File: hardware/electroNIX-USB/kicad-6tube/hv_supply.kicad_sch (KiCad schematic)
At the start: 25 parts, among them Q3 IRLR3110ZPBF

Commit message: electroNIX-USB: apply RFT Z573M data sheet, add tube footprint
The data book confirms the pinout already in the symbol. The tube is
side-view (not top-view), with 13 flying leads on a 9.53 mm circle and
wire 7 at the front. New footprint electronix:Nixie_RFT_Z573M (top
view, wire 7 toward the front edge) is assigned to the tubes.

Tube current: Ik is 1.5-2.5 mA continuous, 12 mA pulse. PCB-036's 10k
anode resistors averaged only ~0.75 mA per tube when multiplexed. Anode
resistors are now 5k6 (4 tubes) and 3k9 (6 tubes), cathode base
resistors 6k8. To carry the extra HV power, the ladder caps go to
2.2 uF and the 6-tube build uses a 22 uH inductor.

Co-Authored-By: Claude Opus 5.5 <noreply@anthropic.com>
Claude-Session: https://claude.ai/code/session_01AFMfevKEKDGbci8uJGhf4W
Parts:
- C13, C14, C15, C16, C17, C18, C19: value 1u 100V -> 2u2 100V
- L1: value 33u WE 7447715330 -> 22u WE 7447715220
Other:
- note added: "Cockcroft-Walton multiplier, 7 x 10MQ100N, 7 x 2u2/100V (PCB-036 used 1u)"
- note removed: "Cockcroft-Walton multiplier, 7 x 10MQ100N, 7 x 1u/100V (as PCB-036)"
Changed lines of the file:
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@@
       (type none))
 )
-  (text "Cockcroft-Walton multiplier, 7 x 10MQ100N, 7 x 1u/100V (as PCB-036)"
+  (text "Cockcroft-Walton multiplier, 7 x 10MQ100N, 7 x 2u2/100V (PCB-036 used 1u)"
     (at 161.27 26.27 0)
     (effects
@@
           (size 1.27 1.27))
         (justify left)))
-    (property "Value" "33u WE 7447715330"
+    (property "Value" "22u WE 7447715220"
       (at 71.12 50.8 0)
       (effects
@@
         (font
           (size 1.27 1.27))))
-    (property "Value" "1u 100V"
+    (property "Value" "2u2 100V"
       (at 199.39 52.07 90)
       (effects
@@
         (font
           (size 1.27 1.27))))
-    (property "Value" "1u 100V"
+    (property "Value" "2u2 100V"
       (at 250.19 52.07 90)
       (effects
@@
         (font
           (size 1.27 1.27))))
-    (property "Value" "1u 100V"
+    (property "Value" "2u2 100V"
       (at 299.72 52.07 90)
       (effects
@@
         (font
           (size 1.27 1.27))))
-    (property "Value" "1u 100V"
+    (property "Value" "2u2 100V"
       (at 350.52 52.07 90)
       (effects
@@
         (font
           (size 1.27 1.27))))
-    (property "Value" "1u 100V"
+    (property "Value" "2u2 100V"
       (at 224.79 97.79 90)
       (effects
@@
         (font
           (size 1.27 1.27))))
-    (property "Value" "1u 100V"
+    (property "Value" "2u2 100V"
       (at 275.59 97.79 90)
       (effects
@@
         (font
           (size 1.27 1.27))))
-    (property "Value" "1u 100V"
+    (property "Value" "2u2 100V"
       (at 325.12 97.79 90)
       (effects

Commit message: electroNIX-USB: drop all switches, regroup board placement by circuit
- No RESET/BOOT/SET: the firmware reads no button, and the CH340C
  DTR/RTS auto-reset handles flashing. SET's pull-up and cap are gone.
- Boost converter is a compact loop (input caps -> L1 -> FET tab) feeding
  the multiplier columns in chain order.
- ESP32: 3V3 decoupling at pin 2, EN RC at pin 3, HV feedback divider and
  clamp at IO35; auto-reset between the CH340C and the module's UART pins.
- Front band spread out: output cap + KBIAS left, cathode row, one anode
  cluster under each tube.
- 6-tube board placed too (150 x 66 mm). Both boards unrouted.

Co-Authored-By: Claude Opus 5.5 <noreply@anthropic.com>
Claude-Session: https://claude.ai/code/session_01AFMfevKEKDGbci8uJGhf4W
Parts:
- removed C21: 100n, Capacitor_SMD:C_0805_2012Metric, symbol Device:C
- removed R12: 6k2, Resistor_SMD:R_0805_2012Metric, symbol Device:R
- added C10: 22u 10V, Capacitor_SMD:C_1206_3216Metric, symbol Device:C
- added R8: 10R, Resistor_SMD:R_0805_2012Metric, symbol Device:R
- C11: value 22u 10V -> 100n; footprint Capacitor_SMD:C_1206_3216Metric -> Capacitor_SMD:C_0805_2012Metric
- C12: value 100n -> 2u2 100V; footprint Capacitor_SMD:C_0805_2012Metric -> Capacitor_SMD:C_1210_3225Metric
- C19: value 2u2 100V -> 2u2 250V; footprint Capacitor_SMD:C_1210_3225Metric -> Capacitor_THT:CP_Radial_D6.3mm_P2.50mm; symbol Device:C -> Device:C_Polarized
- C20: value 2u2 250V -> 100n; footprint Capacitor_THT:CP_Radial_D6.3mm_P2.50mm -> Capacitor_SMD:C_0805_2012Metric; symbol Device:C_Polarized -> Device:C
- R10: value 10k -> 430k; footprint Resistor_SMD:R_0805_2012Metric -> Resistor_SMD:R_1206_3216Metric
- R11: value 430k -> 6k2; footprint Resistor_SMD:R_1206_3216Metric -> Resistor_SMD:R_0805_2012Metric
- R9: value 10R -> 10k
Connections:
- net +170V: now also C12.1, C19.1, R10.1; no longer C13.1, C20.1, R11.1
- net +5V: now also C10.1; no longer C12.1
- net CW_B1: now also C17.2, C18.1; no longer C18.2, C19.1
- net CW_B2: now also C16.2, C17.1; no longer C17.2, C18.1
- net CW_B3: now also C16.1; no longer C17.1
- net CW_T1: now also C14.2, C15.1; no longer C15.2, C16.1
- net CW_T2: now also C13.2, C14.1; no longer C14.2, C15.1
- net CW_T3: now also C12.2, C13.1; no longer C13.2, C14.1
- net GND: now also C15.2, C19.2, R11.2, R9.2, C10.2; no longer C12.2, C16.2, R10.2
- net HV_SW: now also C18.2; no longer C19.2
- net KOMP_170V: now also C20.1, R10.2, R11.1; no longer R11.2
- net PWM: now also R8.1; no longer R10.1
- net at Q3.1 (G): now also R8.2; no longer R9.2
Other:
- moved on the sheet: C11, C12, C13, C14, C15, C16, C17, C18, R10, R11, R9
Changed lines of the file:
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@@
     (on_board yes)
     (dnp no)
-    (property "Reference" "C11"
+    (property "Reference" "C10"
       (at 36.83 58.42 0)
       (effects
@@
       (project "electroNIX-USB"
         (path "/af167dc7-e2c9-570c-bdf4-28156a519677/f6fa350a-459e-5361-98c1-1f12d068c3cb"
-          (reference "C11")
+          (reference "C10")
           (unit 1)))))
   (symbol
@@
     (on_board yes)
     (dnp no)
-    (property "Reference" "C12"
+    (property "Reference" "C11"
       (at 48.26 58.42 0)
       (effects
@@
       (project "electroNIX-USB"
         (path "/af167dc7-e2c9-570c-bdf4-28156a519677/f6fa350a-459e-5361-98c1-1f12d068c3cb"
-          (reference "C12")
+          (reference "C11")
           (unit 1)))))
   (symbol
@@
     (on_board yes)
     (dnp no)
-    (property "Reference" "R9"
+    (property "Reference" "R8"
       (at 91.44 77.47 90)
       (effects
@@
       (project "electroNIX-USB"
         (path "/af167dc7-e2c9-570c-bdf4-28156a519677/f6fa350a-459e-5361-98c1-1f12d068c3cb"
-          (reference "R9")
+          (reference "R8")
           (unit 1)))))
   (symbol
@@
     (on_board yes)
     (dnp no)
-    (property "Reference" "R10"
+    (property "Reference" "R9"
       (at 86.36 93.98 0)
       (effects
@@
       (project "electroNIX-USB"
         (path "/af167dc7-e2c9-570c-bdf4-28156a519677/f6fa350a-459e-5361-98c1-1f12d068c3cb"
-          (reference "R10")
+          (reference "R9")
           (unit 1)))))
   (symbol
@@
     (on_board yes)
     (dnp no)
-    (property "Reference" "C13"
+    (property "Reference" "C12"
       (at 199.39 46.99 90)
       (effects
@@
       (project "electroNIX-USB"
         (path "/af167dc7-e2c9-570c-bdf4-28156a519677/f6fa350a-459e-5361-98c1-1f12d068c3cb"
-          (reference "C13")
+          (reference "C12")
           (unit 1)))))
   (symbol
@@
     (on_board yes)
     (dnp no)
-    (property "Reference" "C14"
+    (property "Reference" "C13"
       (at 250.19 46.99 90)
       (effects
@@
       (project "electroNIX-USB"
         (path "/af167dc7-e2c9-570c-bdf4-28156a519677/f6fa350a-459e-5361-98c1-1f12d068c3cb"
-          (reference "C14")
+          (reference "C13")
           (unit 1)))))
   (symbol
@@
     (on_board yes)
     (dnp no)
-    (property "Reference" "C15"
+    (property "Reference" "C14"
       (at 299.72 46.99 90)
       (effects
@@
       (project "electroNIX-USB"
         (path "/af167dc7-e2c9-570c-bdf4-28156a519677/f6fa350a-459e-5361-98c1-1f12d068c3cb"
-          (reference "C15")
+          (reference "C14")
           (unit 1)))))
   (symbol
@@
     (on_board yes)
     (dnp no)
-    (property "Reference" "C16"
+    (property "Reference" "C15"
       (at 350.52 46.99 90)
       (effects
@@
       (project "electroNIX-USB"
         (path "/af167dc7-e2c9-570c-bdf4-28156a519677/f6fa350a-459e-5361-98c1-1f12d068c3cb"
-          (reference "C16")
+          (reference "C15")
           (unit 1)))))
   (symbol
@@
     (on_board yes)
     (dnp no)
-    (property "Reference" "C17"
+    (property "Reference" "C16"
       (at 224.79 92.71 90)
       (effects
@@
       (project "electroNIX-USB"
         (path "/af167dc7-e2c9-570c-bdf4-28156a519677/f6fa350a-459e-5361-98c1-1f12d068c3cb"
-          (reference "C17")
+          (reference "C16")
           (unit 1)))))
   (symbol
@@
     (on_board yes)
     (dnp no)
-    (property "Reference" "C18"
+    (property "Reference" "C17"
       (at 275.59 92.71 90)
       (effects
@@
       (project "electroNIX-USB"
         (path "/af167dc7-e2c9-570c-bdf4-28156a519677/f6fa350a-459e-5361-98c1-1f12d068c3cb"
-          (reference "C18")
+          (reference "C17")
           (unit 1)))))
   (symbol
@@
     (on_board yes)
     (dnp no)
-    (property "Reference" "C19"
+    (property "Reference" "C18"
       (at 325.12 92.71 90)
       (effects
@@
       (project "electroNIX-USB"
         (path "/af167dc7-e2c9-570c-bdf4-28156a519677/f6fa350a-459e-5361-98c1-1f12d068c3cb"
-          (reference "C19")
+          (reference "C18")
           (unit 1)))))
   (symbol
@@
     (on_board yes)
     (dnp no)
-    (property "Reference" "C20"
+    (property "Reference" "C19"
       (at 45.72 163.83 0)
       (effects
@@
       (project "electroNIX-USB"
         (path "/af167dc7-e2c9-570c-bdf4-28156a519677/f6fa350a-459e-5361-98c1-1f12d068c3cb"
-          (reference "C20")
+          (reference "C19")
           (unit 1)))))
   (symbol
@@
     (on_board yes)
     (dnp no)
-    (property "Reference" "R11"
+    (property "Reference" "R10"
       (at 101.6 158.75 0)
       (effects
@@
       (project "electroNIX-USB"
         (path "/af167dc7-e2c9-570c-bdf4-28156a519677/f6fa350a-459e-5361-98c1-1f12d068c3cb"
-          (reference "R11")
+          (reference "R10")
           (unit 1)))))
   (symbol
@@
     (on_board yes)
     (dnp no)
-    (property "Reference" "R12"
+    (property "Reference" "R11"
       (at 101.6 179.07 0)
       (effects
@@
       (project "electroNIX-USB"
         (path "/af167dc7-e2c9-570c-bdf4-28156a519677/f6fa350a-459e-5361-98c1-1f12d068c3cb"
-          (reference "R12")
+          (reference "R11")
           (unit 1)))))
   (symbol
@@
     (on_board yes)
     (dnp no)
-    (property "Reference" "C21"
+    (property "Reference" "C20"
       (at 116.84 173.99 0)
       (effects
@@
       (project "electroNIX-USB"
         (path "/af167dc7-e2c9-570c-bdf4-28156a519677/f6fa350a-459e-5361-98c1-1f12d068c3cb"
-          (reference "C21")
-          (unit 1)))))
-  (symbol
+          (reference "C20")
+          (unit 1)))))
+  (symbol

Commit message: electroNIX-USB: boost gate pull-down gate-to-source as on PCB-036
R45 on PCB-036 pulls the FET gate (after the 10R) to GND; ours sat on
the IO2 side. Move it to the gate and place it at the gate pad. Add a
note listing what was checked against the PCB-036 schematic.

Co-Authored-By: Claude Opus 5.5 <noreply@anthropic.com>
Claude-Session: https://claude.ai/code/session_01AFMfevKEKDGbci8uJGhf4W
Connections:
- net PWM: no longer R9.1
- net at Q3.1 (G), R8.2: now also R9.1
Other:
- note added: "IO2 drives the logic-level FET directly, 32 kHz, duty clamped to ~41 % by firmware (HV_DUTY_MAX). 10k gate-source keeps the FET off (and IO2 low) during boot."
- note removed: "IO2 drives the logic-level FET directly, 32 kHz, duty clamped to ~41 % by firmware (HV_DUTY_MAX). 10k keeps the gate (and IO2) low during boot."
- moved on the sheet: R9
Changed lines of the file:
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@@
   (wire
     (pts
-      (xy 85.09 91.44)
-      (xy 85.09 88.9))
-    (stroke
-      (width 0)
-      (type default))
-)
-  (wire
-    (pts
-      (xy 85.09 99.06)
-      (xy 85.09 101.6))
-    (stroke
-      (width 0)
-      (type default))
+      (xy 95.25 87.63)
+      (xy 95.25 90.17))
+    (stroke
+      (width 0)
+      (type default))
+)
+  (junction
+    (at 94.92 80.01)
+    (diameter 0)
+    (color 0 0 0 0)
 )
   (wire
@@
     (property "Intersheetrefs" "${INTERSHEET_REFS}"
       (at 85.09 80.01 0)
-      (effects
-        (font
-          (size 1.27 1.27)) hide)))
-  (global_label "PWM"
-    (shape passive)
-    (at 85.09 88.9 90)
-    (fields_autoplaced)
-    (effects
-      (font
-        (size 1.27 1.27))
-      (justify left))
-    (property "Intersheetrefs" "${INTERSHEET_REFS}"
-      (at 85.09 88.9 0)
       (effects
         (font
@@
       (justify left top))
 )
-  (text "IO2 drives the logic-level FET directly, 32 kHz,\nduty clamped to ~41 % by firmware (HV_DUTY_MAX).\n10k keeps the gate (and IO2) low during boot."
+  (text "IO2 drives the logic-level FET directly, 32 kHz,\nduty clamped to ~41 % by firmware (HV_DUTY_MAX).\n10k gate-source keeps the FET off (and IO2 low) during boot."
     (at 25 105 0)
     (effects
@@
   (symbol
     (lib_id "power:GND")
-    (at 85.09 101.6 0)
+    (at 95.25 90.17 0)
     (unit 1)
     (in_bom yes)
@@
     (dnp no)
     (property "Reference" "#PWR4011"
-      (at 85.09 101.6 0)
+      (at 95.25 90.17 0)
       (effects
         (font
           (size 1.27 1.27)) hide))
     (property "Value" "GND"
-      (at 85.09 104.8 0)
+      (at 95.25 93.37 0)
       (effects
         (font
           (size 1.27 1.27))))
     (property "Footprint" ""
-      (at 85.09 101.6 0)
+      (at 95.25 90.17 0)
       (effects
         (font
           (size 1.27 1.27)) hide))
     (property "Datasheet" ""
-      (at 85.09 101.6 0)
+      (at 95.25 90.17 0)
       (effects
         (font
@@
   (symbol
     (lib_id "Device:R")
-    (at 85.09 95.25 0)
+    (at 95.25 83.82 0)
     (unit 1)
     (in_bom yes)
@@
     (dnp no)
     (property "Reference" "R9"
-      (at 86.36 93.98 0)
+      (at 96.52 82.55 0)
       (effects
         (font
@@
         (justify left)))
     (property "Value" "10k"
-      (at 86.36 96.52 0)
+      (at 96.52 85.09 0)
       (effects
         (font
@@
         (justify left)))
     (property "Footprint" "Resistor_SMD:R_0805_2012Metric"
-      (at 85.09 95.25 0)
+      (at 95.25 83.82 0)
       (effects
         (font
@@
         (justify left) hide))
     (property "Datasheet" "~"
-      (at 85.09 95.25 0)
-      (effects
-        (font
+      (at 95.25 83.82 0)
+      (effects
+        (font

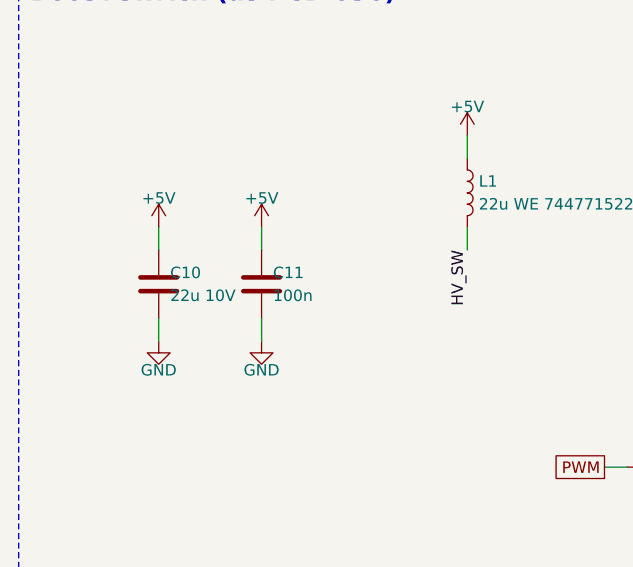
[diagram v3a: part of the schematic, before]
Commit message: electroNIX-USB: tantalum bulk caps on the 5 V input and boost input
Back to PCB-036's 22 uF/35 V tantalum (7343 D case) for the boost input
and use the same part for the USB-C bulk cap. It holds its value at 5 V,
unlike a small MLCC, and its ESR damps hot-plug ringing on the cable.
The 100 nF ceramics stay. Placement adjusted around the larger parts.

Co-Authored-By: Claude Opus 5.5 <noreply@anthropic.com>
Claude-Session: https://claude.ai/code/session_01AFMfevKEKDGbci8uJGhf4W
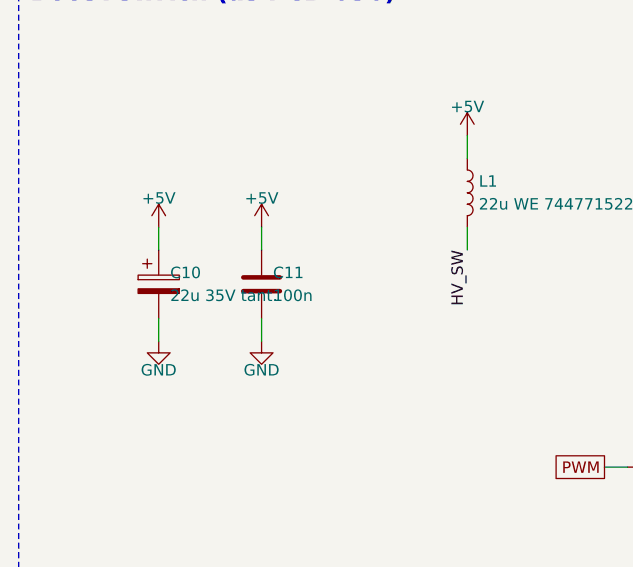
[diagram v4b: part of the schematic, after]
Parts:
- C10: value 22u 10V -> 22u 35V tant.; footprint Capacitor_SMD:C_1206_3216Metric -> Capacitor_Tantalum_SMD:CP_EIA-7343-31_Kemet-D; symbol Device:C -> Device:C_Polarized
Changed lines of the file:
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@@
           (unit 1)))))
   (symbol
-    (lib_id "Device:C")
+    (lib_id "Device:C_Polarized")
     (at 35.56 59.69 0)
     (unit 1)
@@
           (size 1.27 1.27))
         (justify left)))
-    (property "Value" "22u 10V"
+    (property "Value" "22u 35V tant."
       (at 36.83 60.96 0)
       (effects
@@
           (size 1.27 1.27))
         (justify left)))
-    (property "Footprint" "Capacitor_SMD:C_1206_3216Metric"
+    (property "Footprint" "Capacitor_Tantalum_SMD:CP_EIA-7343-31_Kemet-D"
       (at 35.56 59.69 0)
       (effects

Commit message: electroNIX-USB: lay the 170 V output electrolytic flat
New footprint CP_Radial_D8mm_P2.50mm_Lying (2.5 mm leads, keep-clear for
a body up to 8 x 12.5 mm folded flat). C19 now runs along the left edge
toward the front; KBIAS parts and the cathode row moved right to clear it.

Co-Authored-By: Claude Opus 5.5 <noreply@anthropic.com>
Claude-Session: https://claude.ai/code/session_01AFMfevKEKDGbci8uJGhf4W
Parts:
- C19: footprint Capacitor_THT:CP_Radial_D6.3mm_P2.50mm -> electronix:CP_Radial_D8mm_P2.50mm_Lying
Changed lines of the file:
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@@
           (size 1.27 1.27))
         (justify left)))
-    (property "Footprint" "Capacitor_THT:CP_Radial_D6.3mm_P2.50mm"
+    (property "Footprint" "electronix:CP_Radial_D8mm_P2.50mm_Lying"
       (at 44.45 165.1 0)
       (effects
